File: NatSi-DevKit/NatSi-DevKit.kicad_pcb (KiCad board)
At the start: 4 copper layers, 25.4 x 62.5 mm, 42 parts, among them J1 USB_TypeC, J2 Conn_01x22_Pin, J3 Conn_01x22_Pin, J4 MEM2067-02-180-00-A_REVB, SW1 SW_Push, SW2 SW_Push, SW3 SW_Push, U1 USBLC6-2SC6, U2 ESP32-S3-WROOM-1, U3 NCP1117-3.3_SOT223

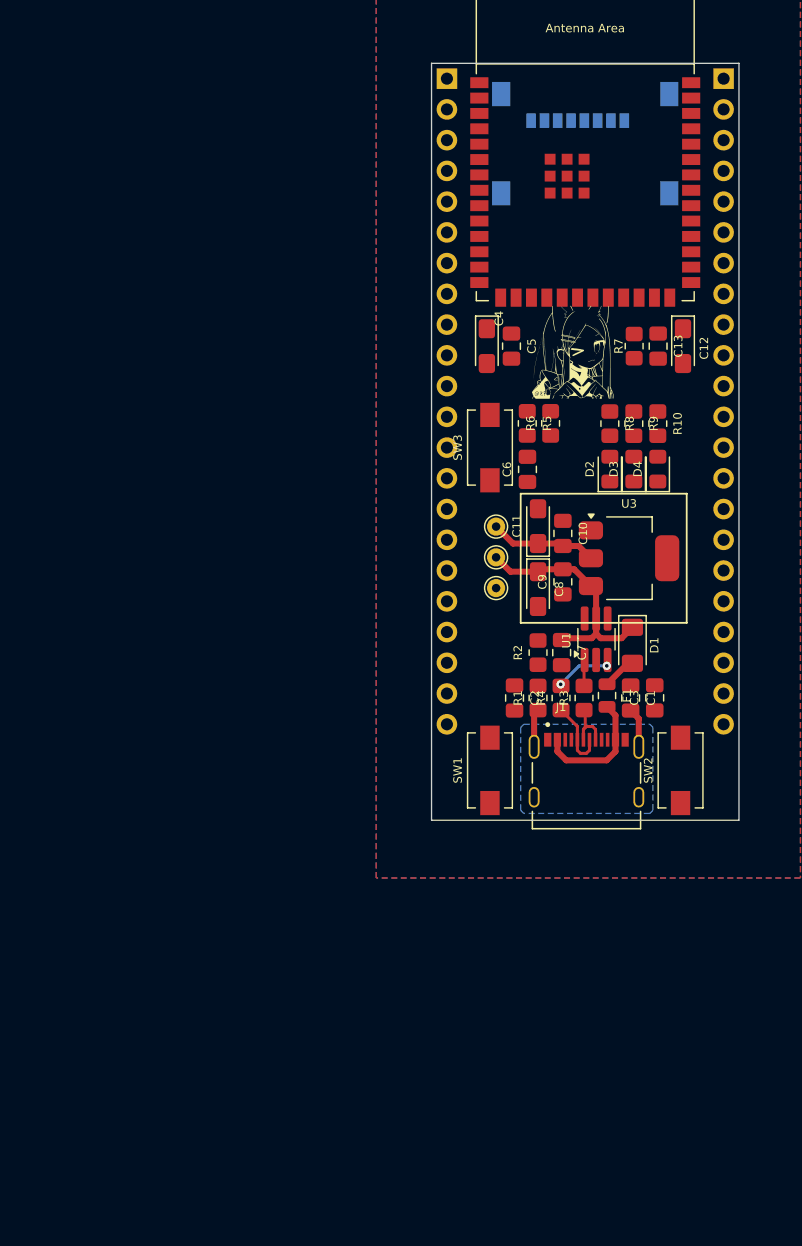
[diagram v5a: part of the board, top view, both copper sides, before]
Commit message: PCB routing update
fuuyah a lot of pain to do these routes, Im also a shitty person.
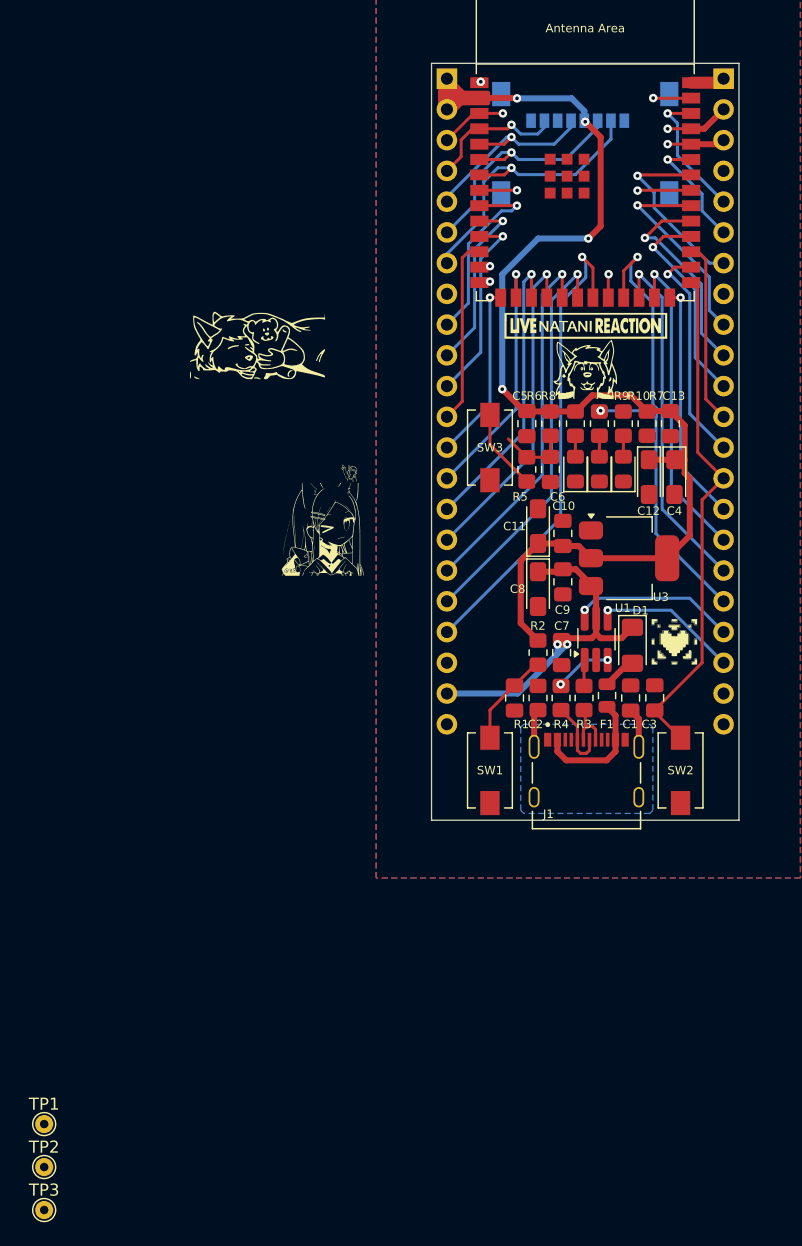
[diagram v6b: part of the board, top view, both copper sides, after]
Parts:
- added TP5: TestPoint, sumec_graphic:NAT_PFP_IMG, F.Cu at (234.3, 79.8)
- added TP6: TestPoint, sumec_graphic:FLO_FRONT_C_IMG, F.Cu at (228.5, 56.6)
- added TP7: TestPoint, sumec_graphic:LIVE_NAT_REACTION_NEG, F.Cu at (226.9, 53.7)
- added TP8: TestPoint, sumec_graphic:FLO_SLEEP_IMG, F.Cu at (199.7, 52.2)
- added TP9: TestPoint, sumec_graphic:FLO_POINTING_IMG, F.Cu at (206.6, 62.2)
- moved TP3 63.5 mm to (182.2, 126.8)
- moved TP2 62.7 mm to (182.2, 123.2)
- moved TP1 61.9 mm to (182.2, 119.7)
- moved TP4 25.3 mm to (208.3, 70.5)
- moved C4 18.9 mm to (234.3, 66.2)
- moved C12 11.2 mm to (232.2, 66.2)
- moved C5 6.53 mm to (222.1, 61.8)
- moved R7 6.49 mm to (232.1, 61.8)
- moved C13 6.48 mm to (234.0, 61.8)
- moved R5 3.80 mm to (222.1, 65.6), turned to 90 degrees
- moved D2 2.84 mm to (226.1, 65.5)
- moved D3 2.84 mm to (228.1, 65.5)
- moved D4 2.84 mm to (230.1, 65.5)
- moved R10 2.84 mm to (230.1, 61.8)
- moved R8 2.84 mm to (226.1, 61.8)
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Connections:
- net Net-(R5-Pad1) renamed /BUTTON
- C3 pad 1: BOOT -> IO00_BOOT
- C6 pad 2: BT1 -> IO8_BT
- J2 pad 1: unconnected-(J2-Pin_1-Pad1) -> +3V3
- J2 pad 10: unconnected-(J2-Pin_10-Pad10) -> IO17
- J2 pad 11: unconnected-(J2-Pin_11-Pad11) -> IO18
- J2 pad 12: unconnected-(J2-Pin_12-Pad12) -> IO8_BT
- J2 pad 13: unconnected-(J2-Pin_13-Pad13) -> IO03
- J2 pad 14: unconnected-(J2-Pin_14-Pad14) -> IO46
- J2 pad 15: unconnected-(J2-Pin_15-Pad15) -> IO09
- J2 pad 16: unconnected-(J2-Pin_16-Pad16) -> IO10
- J2 pad 17: unconnected-(J2-Pin_17-Pad17) -> IO11
- J2 pad 18: unconnected-(J2-Pin_18-Pad18) -> IO12
- J2 pad 19: unconnected-(J2-Pin_19-Pad19) -> IO13
- J2 pad 2: unconnected-(J2-Pin_2-Pad2) -> +3V3
- J2 pad 20: unconnected-(J2-Pin_20-Pad20) -> IO14
- J2 pad 21: unconnected-(J2-Pin_21-Pad21) -> +5V
- J2 pad 22: unconnected-(J2-Pin_22-Pad22) -> GND
- J2 pad 3: unconnected-(J2-Pin_3-Pad3) -> EN
- J2 pad 4: unconnected-(J2-Pin_4-Pad4) -> IO04_MISO
- J2 pad 5: unconnected-(J2-Pin_5-Pad5) -> IO05_CLK
- J2 pad 6: unconnected-(J2-Pin_6-Pad6) -> IO06_MOSI
- J2 pad 7: unconnected-(J2-Pin_7-Pad7) -> IO07_~{CS}
- J2 pad 8: unconnected-(J2-Pin_8-Pad8) -> IO15
- J2 pad 9: unconnected-(J2-Pin_9-Pad9) -> IO16
- J3 pad 1: unconnected-(J3-Pin_1-Pad1) -> GND
- J3 pad 10: unconnected-(J3-Pin_10-Pad10) -> IO38
- J3 pad 11: unconnected-(J3-Pin_11-Pad11) -> IO37
- J3 pad 12: unconnected-(J3-Pin_12-Pad12) -> IO36
- J3 pad 13: unconnected-(J3-Pin_13-Pad13) -> IO35
- J3 pad 14: unconnected-(J3-Pin_14-Pad14) -> IO00_BOOT
- J3 pad 15: unconnected-(J3-Pin_15-Pad15) -> IO45
- J3 pad 16: unconnected-(J3-Pin_16-Pad16) -> IO48
- J3 pad 17: unconnected-(J3-Pin_17-Pad17) -> IO47_LED
- J3 pad 18: unconnected-(J3-Pin_18-Pad18) -> IO21_LED
- J3 pad 19: unconnected-(J3-Pin_19-Pad19) -> IO20_D+
- J3 pad 2: unconnected-(J3-Pin_2-Pad2) -> TXD0
- J3 pad 20: unconnected-(J3-Pin_20-Pad20) -> IO19_D-
- J3 pad 21: unconnected-(J3-Pin_21-Pad21) -> GND
- J3 pad 22: unconnected-(J3-Pin_22-Pad22) -> GND
- J3 pad 3: unconnected-(J3-Pin_3-Pad3) -> RXD0
- J3 pad 4: unconnected-(J3-Pin_4-Pad4) -> IO01
- J3 pad 5: unconnected-(J3-Pin_5-Pad5) -> IO02
- J3 pad 6: unconnected-(J3-Pin_6-Pad6) -> IO42
- J3 pad 7: unconnected-(J3-Pin_7-Pad7) -> IO41
- J3 pad 8: unconnected-(J3-Pin_8-Pad8) -> IO40
- J3 pad 9: unconnected-(J3-Pin_9-Pad9) -> IO39
- J4 pad 2: IO10_~{CS} -> IO07_~{CS}
- J4 pad 3: IO11_MOSI -> IO06_MOSI
- J4 pad 5: IO12_CLK -> IO05_CLK
- J4 pad 7: IO13_MISO -> IO04_MISO
- R10 pad 1: LED2 -> IO47_LED
- R5 pad 2: BT1 -> IO8_BT
- R6 pad 1: BT1 -> IO8_BT
- R7 pad 1: IO10_~{CS} -> IO07_~{CS}
- R9 pad 1: LED1 -> IO21_LED
- SW2 pad 2: BOOT -> IO00_BOOT
- U1 pad 4: D- -> IO19_D-
- U1 pad 6: D+ -> IO20_D+
- U2 pad 12: IO08 -> IO8_BT
- U2 pad 13: D- -> IO19_D-
- U2 pad 14: D+ -> IO20_D+
- U2 pad 16: IO42 -> IO46
- U2 pad 18: IO10_~{CS} -> IO10
- U2 pad 19: IO11_MOSI -> IO11
- U2 pad 20: IO12_CLK -> IO12
- U2 pad 21: IO13_MISO -> IO13
- U2 pad 23: IO21 -> IO21_LED
- U2 pad 24: IO47 -> IO47_LED
- U2 pad 27: BOOT -> IO00_BOOT
- U2 pad 36: RX -> RXD0
- U2 pad 37: TX -> TXD0
- U2 pad 4: IO04 -> IO04_MISO
- U2 pad 5: IO05 -> IO05_CLK
- U2 pad 6: IO06 -> IO06_MOSI
- U2 pad 7: IO07 -> IO07_~{CS}
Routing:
- net +3V3: track 8.92 -> 91.1 mm, vias 0 -> 4
- net IO00_BOOT: track 0.00 -> 42.0 mm
- net IO21_LED: track 0.00 -> 41.8 mm, vias 0 -> 2
- net IO13: track 0.00 -> 39.6 mm, vias 0 -> 1
- net IO12: track 0.00 -> 33.4 mm, vias 0 -> 1
- net IO11: track 0.00 -> 30.4 mm, vias 0 -> 1
- net IO47_LED: track 0.00 -> 29.3 mm, vias 0 -> 1
- net IO10: track 0.00 -> 27.3 mm, vias 0 -> 1
- net IO48: track 0.00 -> 26.3 mm, vias 0 -> 1
- net IO07_~{CS}: track 0.00 -> 25.1 mm, vias 0 -> 1
- net IO09: track 0.00 -> 24.2 mm, vias 0 -> 1
- net IO06_MOSI: track 0.00 -> 21.2 mm, vias 0 -> 1
- net IO46: track 0.00 -> 21.2 mm, vias 0 -> 1
- net IO8_BT: track 0.00 -> 21.2 mm
- net IO45: track 0.00 -> 19.8 mm, vias 0 -> 1
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
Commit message: some 3d updates
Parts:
- SW1, SW2, SW3: footprint Button_Switch_SMD:SW_SPST_EVQPE1 -> sumec_brd:SW_SPST_EVQPE1

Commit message: PCB update - traces
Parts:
- removed TP1, TP2, TP3: TestPoint, TestPoint:TestPoint_THTPad_D1.5mm_Drill0.7mm
- J1: footprint sumec_brd:USB_Type_C -> sumec_brd:HRO_TYPE-C-31-M-12
- moved TP5 24.4 mm to (209.9, 80.8)
- moved C2 4.20 mm to (223.0, 80.7), turned to 90 degrees
- moved U1 4.05 mm to (231.9, 79.5)
- moved R2 1.89 mm to (224.9, 80.7)
- moved C7 1.87 mm to (226.9, 80.7)
- moved D1 1.87 mm to (229.0, 80.1)
- moved J1 0.19 mm to (227.1, 92.5)
- turned SW3 to -90 degrees
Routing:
- net EN: track 13.3 -> 67.4 mm, vias 1 -> 3
- net IO14: track 2.14 -> 40.5 mm
- net IO21_LED: track 41.8 -> 3.83 mm, vias 2 -> 1
- net IO20_D+: track 14.7 -> 48.1 mm
- net IO19_D-: track 13.0 -> 39.9 mm
- net GND: track 2.82 -> 23.2 mm, vias 1 -> 6
- net IO15: track 3.11 -> 13.5 mm
- net IO40: track 4.44 -> 14.0 mm
- net IO8_BT: track 21.2 -> 28.4 mm, vias 0 -> 1
- net Net-(R4-Pad2): track 4.86 -> 0.14 mm, vias 2 -> 0
- net IO01: track 3.09 -> 7.58 mm
- net /BUTTON: track 7.19 -> 3.09 mm
- net IO41: track 15.3 -> 11.7 mm
- net +3V3: track 91.1 -> 94.3 mm
- net Net-(D1-A): track 2.81 -> 0.00 mm
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- added copper zone on F.Cu, net /SHLD
